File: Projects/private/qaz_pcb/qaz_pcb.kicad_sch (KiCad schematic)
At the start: 2 parts

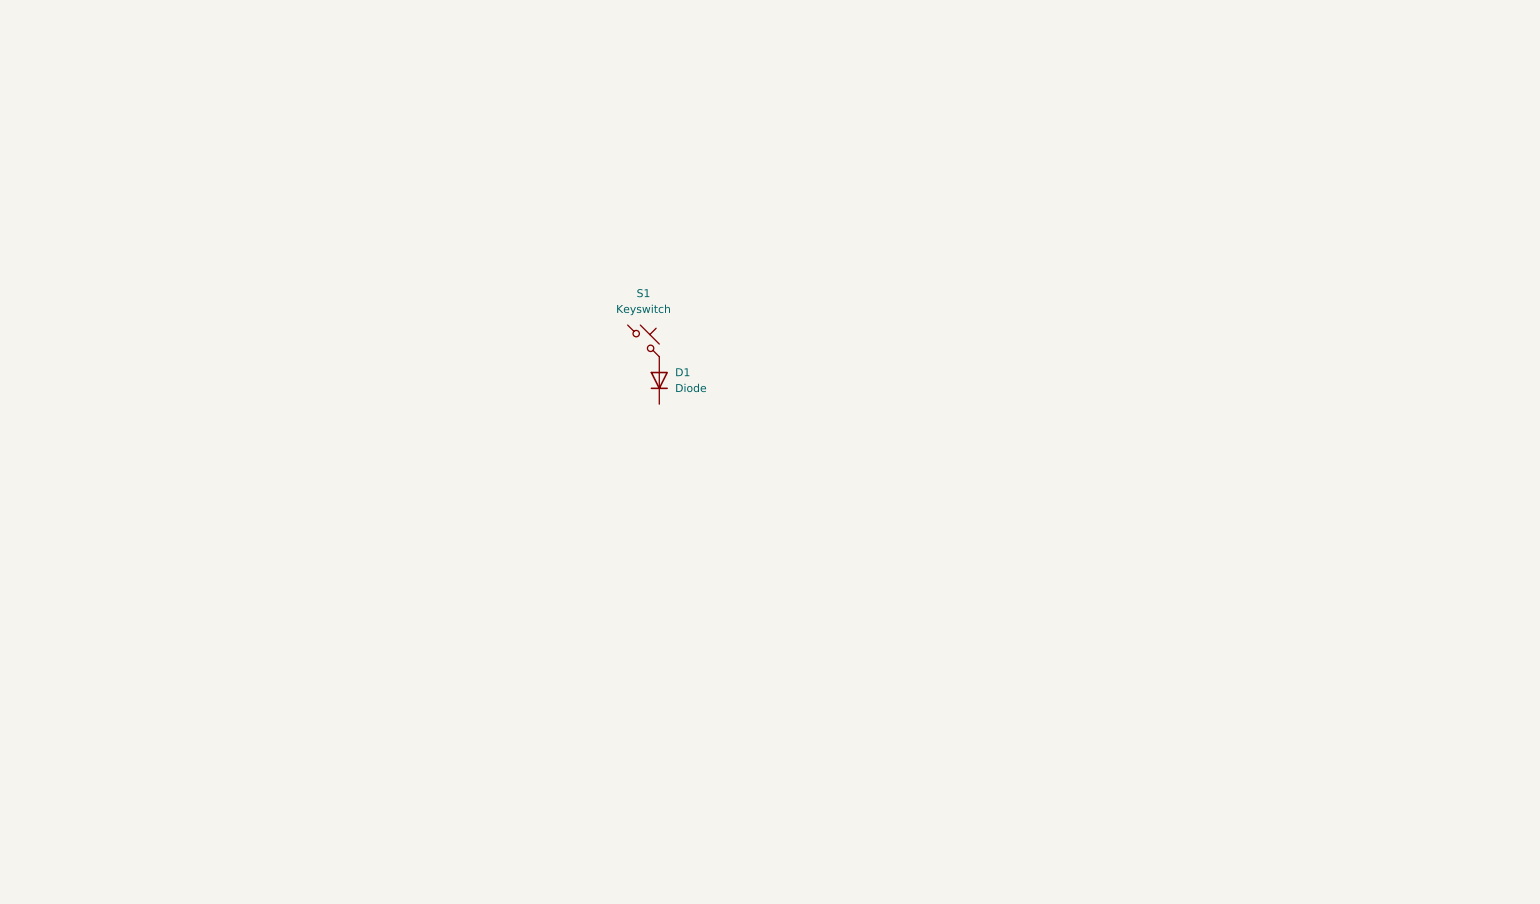
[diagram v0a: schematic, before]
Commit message: update
- aligned everything
- only connections need to be traced
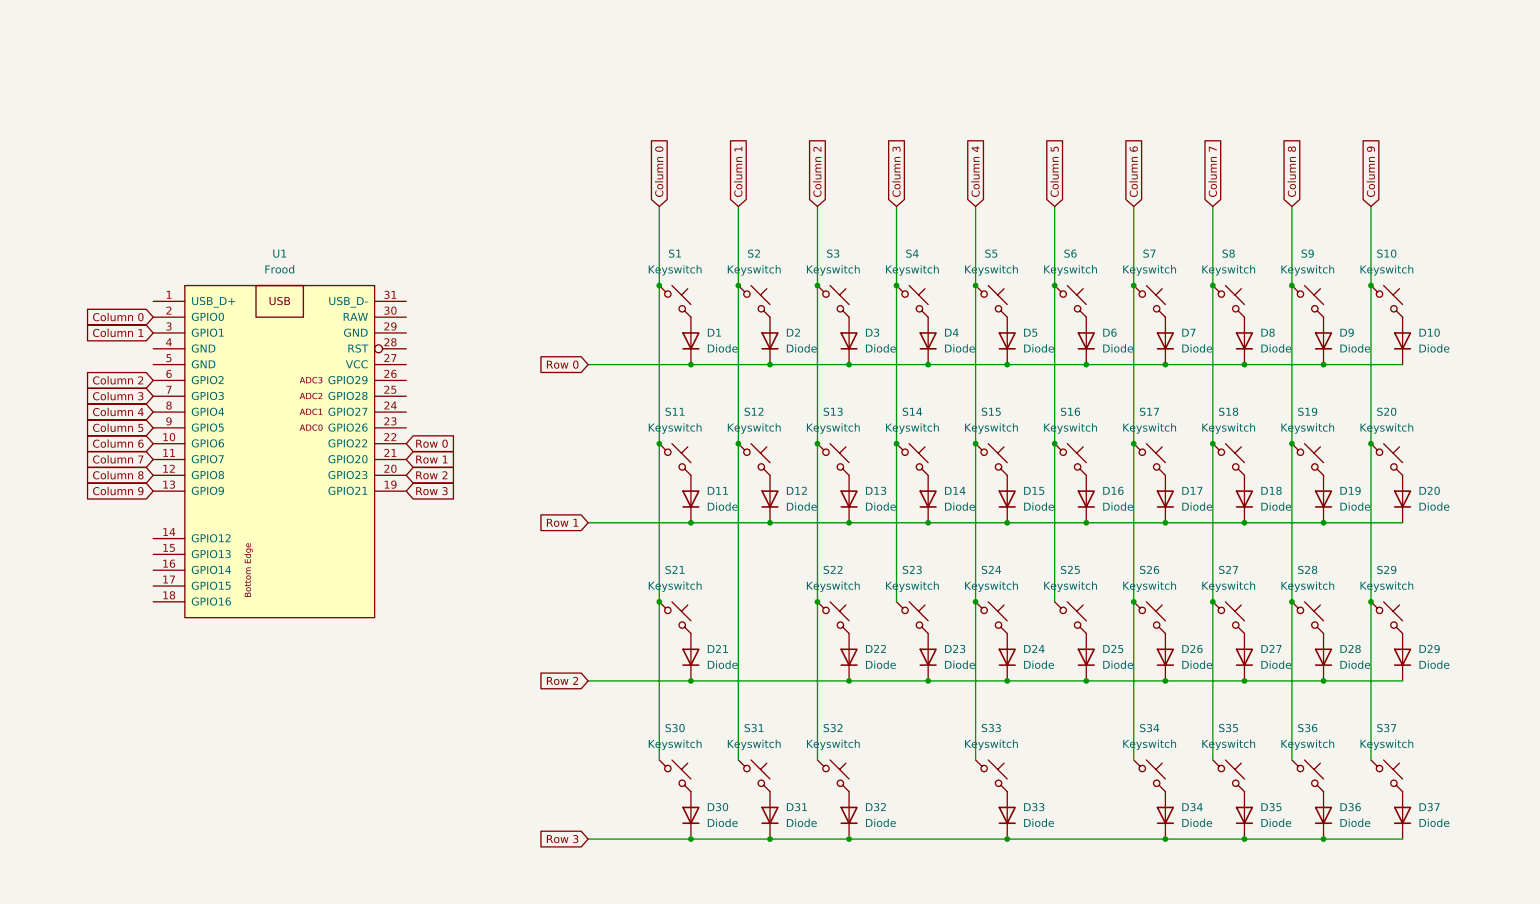
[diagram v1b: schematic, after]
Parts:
- added D10, D11, D12, D13, D14, D15, D16, D17, D18, D19, D2, D20, D21, D22, D23, D24, D25, D26, D27, D28, D29, D3, D30, D31, D32, D33, D34, D35, D36, D37, D4, D5, D6, D7, D8, D9: Diode, ScottoKeebs_Components:Diode_SOD-123, symbol Kunsteak:Placeholder_Diode
- added S10, S11: Keyswitch, ScottoKeebs_Hotswap:Hotswap_MX_1.25u, symbol Kunsteak:Placeholder_Keyswitch
- added S12, S13, S14, S15, S16, S17, S18, S19, S2, S20, S22, S23, S24, S25, S26, S27, S28, S3, S30, S31, S32, S35, S36, S37, S4, S5, S6, S7, S8, S9: Keyswitch, ScottoKeebs_Hotswap:Hotswap_MX_1.00u, symbol Kunsteak:Placeholder_Keyswitch
- added S21: Keyswitch, ScottoKeebs_Hotswap:Hotswap_MX_1.75u, symbol Kunsteak:Placeholder_Keyswitch
- added S29: Keyswitch, ScottoKeebs_Hotswap:Hotswap_MX_1.50u, symbol Kunsteak:Placeholder_Keyswitch
- added S33: Keyswitch, ScottoKeebs_Hotswap:Hotswap_MX_2.25u, symbol Kunsteak:Placeholder_Keyswitch
- added S34: Keyswitch, ScottoKeebs_Hotswap:Hotswap_MX_2.00u, symbol Kunsteak:Placeholder_Keyswitch
- added U1: Frood, footprints:Frood_PinHeader_2x13+5_P2.54mm_Labels_Top, symbol 42Keebs:Frood
- D1: footprint (none) -> ScottoKeebs_Components:Diode_SOD-123
- S1: footprint (none) -> ScottoKeebs_Hotswap:Hotswap_MX_1.00u
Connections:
- net Column 0: now reaches S1.1
- net Column 0: now also S11.1, S21.1, S30.1, U1.2 (GPIO0)
- net Row 0: now reaches D1.1 (K)
- net Row 0: now also D10.1 (K), D2.1 (K), D3.1 (K), D4.1 (K), D5.1 (K), D6.1 (K), D7.1 (K), D8.1 (K), D9.1 (K), U1.22 (GPIO22)
- new net: D15.2 (A), S15.2
- new net: D8.2 (A), S8.2
- new net: D7.2 (A), S7.2
- new net: D20.2 (A), S20.2
- new net: D35.2 (A), S35.2
- new net: D26.2 (A), S26.2
- new net: D29.2 (A), S29.2
- new net: D22.2 (A), S22.2
- new net: D34.2 (A), S34.2
- new net: D12.2 (A), S12.2
- new net: D27.2 (A), S27.2
- new net: D24.2 (A), S24.2
- new net: D32.2 (A), S32.2
- new net: D9.2 (A), S9.2
- new net: D31.2 (A), S31.2
- new net: D2.2 (A), S2.2
- new net: D5.2 (A), S5.2
- new net: D4.2 (A), S4.2
- new net: D23.2 (A), S23.2
- new net: D10.2 (A), S10.2
- new net: D37.2 (A), S37.2
- new net: D19.2 (A), S19.2
- new net: D28.2 (A), S28.2
- new net: D6.2 (A), S6.2
- new net: D17.2 (A), S17.2
- new net: D25.2 (A), S25.2
- new net: D16.2 (A), S16.2
- new net: D3.2 (A), S3.2
- new net: D36.2 (A), S36.2
- new net: D13.2 (A), S13.2
- new net: D21.2 (A), S21.2
- new net: D30.2 (A), S30.2
- new net: D18.2 (A), S18.2
- new net: D33.2 (A), S33.2
- new net: D14.2 (A), S14.2
- new net: D11.2 (A), S11.2
- new net Column 1: S12.1, S2.1, S31.1, U1.3 (GPIO1)
- new net Column 2: S13.1, S22.1, S3.1, S32.1, U1.6 (GPIO2)
- new net Column 3: S14.1, S23.1, S4.1, U1.7 (GPIO3)
- new net Column 4: S15.1, S24.1, S33.1, S5.1, U1.8 (GPIO4)
- new net Column 5: S16.1, S25.1, S6.1, U1.9 (GPIO5)
- new net Column 6: S17.1, S26.1, S34.1, S7.1, U1.10 (GPIO6)
- new net Column 7: S18.1, S27.1, S35.1, S8.1, U1.11 (GPIO7)
- new net Column 8: S19.1, S28.1, S36.1, S9.1, U1.12 (GPIO8)
- new net Column 9: S10.1, S20.1, S29.1, S37.1, U1.13 (GPIO9)
- new net Row 1: D11.1 (K), D12.1 (K), D13.1 (K), D14.1 (K), D15.1 (K), D16.1 (K), D17.1 (K), D18.1 (K), D19.1 (K), D20.1 (K), U1.21 (GPIO20)
- new net Row 2: D21.1 (K), D22.1 (K), D23.1 (K), D24.1 (K), D25.1 (K), D26.1 (K), D27.1 (K), D28.1 (K), D29.1 (K), U1.20 (GPIO23)
- new net Row 3: D30.1 (K), D31.1 (K), D32.1 (K), D33.1 (K), D34.1 (K), D35.1 (K), D36.1 (K), D37.1 (K), U1.19 (GPIO21)
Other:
- moved on the sheet: D1, S1

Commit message: update
- removed folders and files created with newer versions of KiCAD
- added frood-specific files
- made all the necessary changes in both schematics and pcb editor (footprints)
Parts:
- removed U1: Frood, footprints:Frood_PinHeader_2x13+5_P2.54mm_Labels_Top, symbol 42Keebs:Frood
- added U1: Frood, ScottoKeebs_MCU:Frood_PinHeader_2x13+5_P2.54mm_Labels_Top, symbol 42Keebs2:Frood
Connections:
- net Column 0: now also U1.2 (GPIO0)
- net Column 1: now also U1.3 (GPIO1)
- net Column 2: now also U1.6 (GPIO2)
- net Column 3: now also U1.7 (GPIO3)
- net Column 4: now also U1.8 (GPIO4)
- net Column 5: now also U1.9 (GPIO5)
- net Column 6: now also U1.10 (GPIO6)
- net Column 7: now also U1.11 (GPIO7)
- net Column 8: now also U1.12 (GPIO8)
- net Column 9: now also U1.13 (GPIO9)
- net Row 0: now also U1.22 (GPIO22)
- net Row 1: now also U1.21 (GPIO20)
- net Row 2: now also U1.20 (GPIO23)
- net Row 3: now also U1.19 (GPIO21)

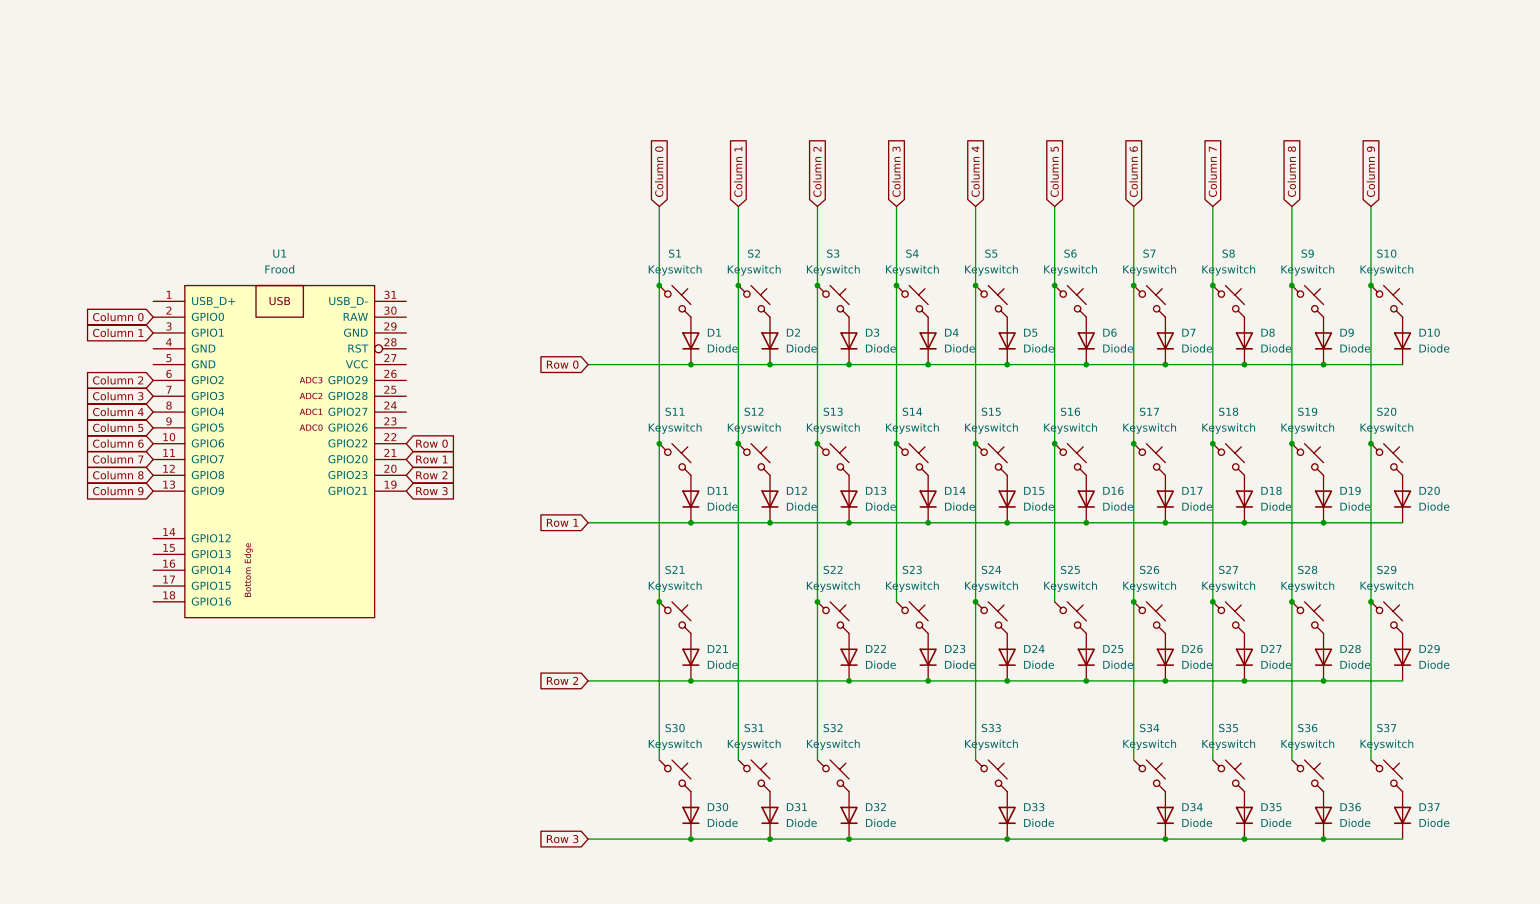
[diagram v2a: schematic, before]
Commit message: Finalised qaz pcb
- finished the traces and connections
- merged all necessary symbols, footprints, and 3d models into the ScottoKicad files and folders
- added rotary encoder for the qaz (with schematic and 3d model)
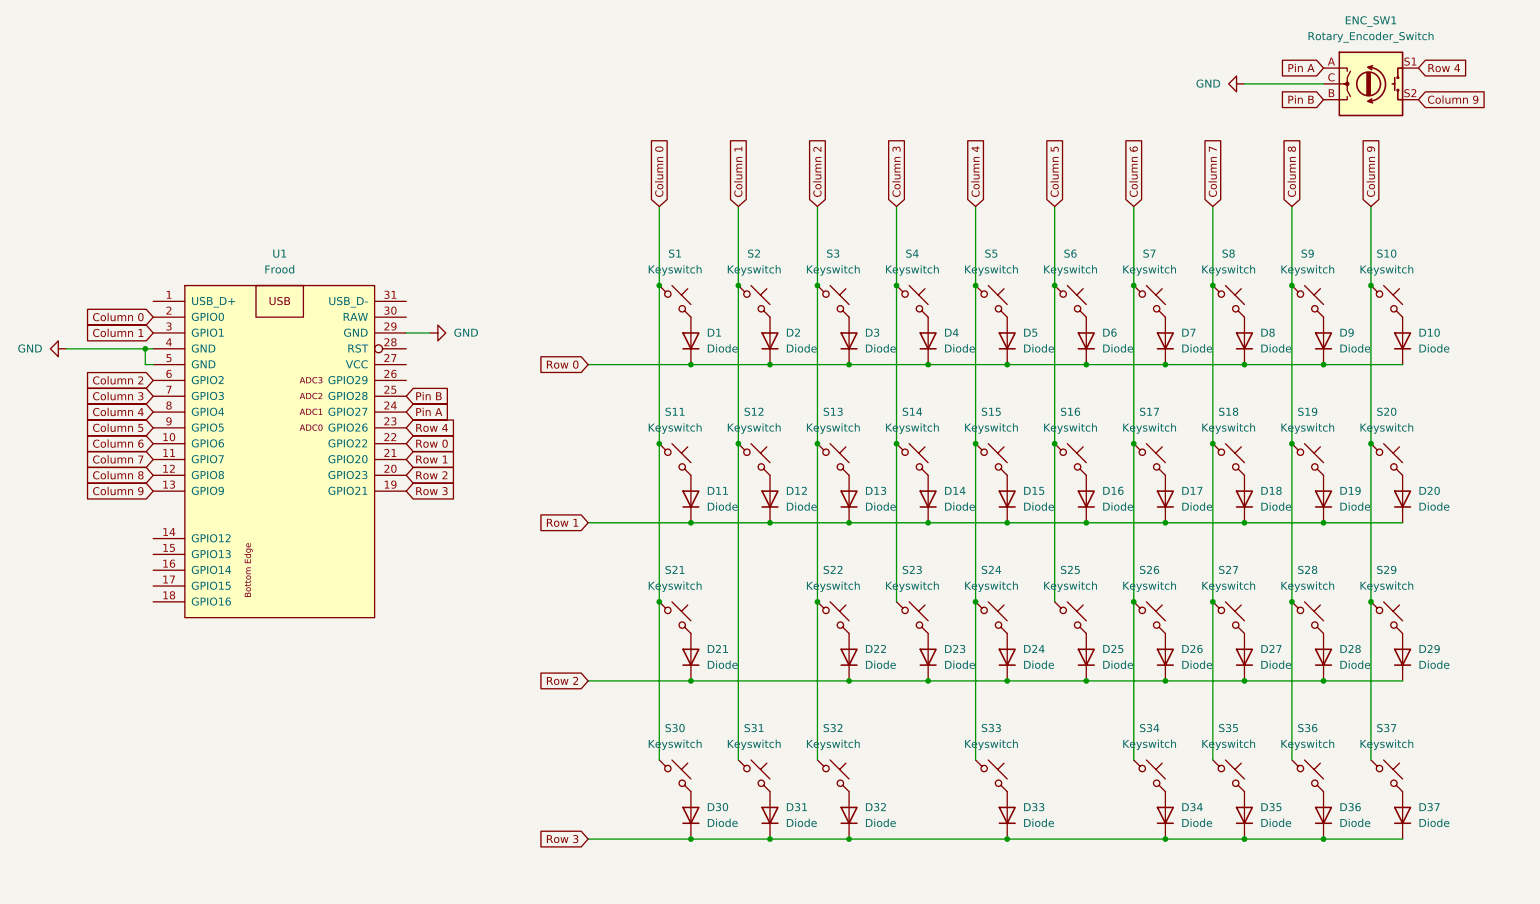
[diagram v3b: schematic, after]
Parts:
- removed U1: Frood, ScottoKeebs_MCU:Frood_PinHeader_2x13+5_P2.54mm_Labels_Top, symbol 42Keebs2:Frood
- added ENC_SW1: Rotary_Encoder_Switch, ScottoKeebs_Components:Rotary_Encoder_PEC11R-4220K-S0024, symbol ScottoKeebs:Rotary_Encoder_Switch
- added U1: Frood, ScottoKeebs_MCU:Frood_PinHeader_2x13+5_P2.54mm_Labels_Top, symbol ScottoKeebs:Frood
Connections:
- net Column 0: now also U1.2 (GPIO0)
- net Column 1: now also U1.3 (GPIO1)
- net Column 2: now also U1.6 (GPIO2)
- net Column 3: now also U1.7 (GPIO3)
- net Column 4: now also U1.8 (GPIO4)
- net Column 5: now also U1.9 (GPIO5)
- net Column 6: now also U1.10 (GPIO6)
- net Column 7: now also U1.11 (GPIO7)
- net Column 8: now also U1.12 (GPIO8)
- net Column 9: now also ENC_SW1.S2, U1.13 (GPIO9)
- net Row 0: now also U1.22 (GPIO22)
- net Row 1: now also U1.21 (GPIO20)
- net Row 2: now also U1.20 (GPIO23)
- net Row 3: now also U1.19 (GPIO21)
- new net GND: ENC_SW1.C, U1.29 (GND), U1.4 (GND), U1.5 (GND)
- new net Pin A: ENC_SW1.A, U1.24 (GPIO27)
- new net Pin B: ENC_SW1.B, U1.25 (GPIO28)
- new net Row 4: ENC_SW1.S1, U1.23 (GPIO26)

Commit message: update
- renamed everything from ScottoKeebs to Kunsteak
- only updated the footprints and symbols relevant to the qaz project (all the other ones will have to be updated once they are used)
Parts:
- D1, D10, D11, D12, D13, D14, D15, D16, D17, D18, D19, D2, D20, D21, D22, D23, D24, D25, D26, D27, D28, D29, D3, D30, D31, D32, D33, D34, D35, D36, D37, D4, D5, D6, D7, D8, D9: footprint ScottoKeebs_Components:Diode_SOD-123 -> Kunsteak_Components:Diode_SOD-123
- ENC_SW1: footprint ScottoKeebs_Components:Rotary_Encoder_PEC11R-4220K-S0024 -> Kunsteak_Components:Rotary_Encoder_PEC11R-4220K-S0024
- S1, S12, S13, S14, S15, S16, S17, S18, S19, S2, S20, S22, S23, S24, S25, S26, S27, S28, S3, S30, S31, S32, S35, S36, S37, S4, S5, S6, S7, S8, S9: footprint ScottoKeebs_Hotswap:Hotswap_MX_1.00u -> Kunsteak_Hotswap:Hotswap_MX_1.00u
- S10, S11: footprint ScottoKeebs_Hotswap:Hotswap_MX_1.25u -> Kunsteak_Hotswap:Hotswap_MX_1.25u
- S21: footprint ScottoKeebs_Hotswap:Hotswap_MX_1.75u -> Kunsteak_Hotswap:Hotswap_MX_1.75u
- S29: footprint ScottoKeebs_Hotswap:Hotswap_MX_1.50u -> Kunsteak_Hotswap:Hotswap_MX_1.00u
- S33: footprint ScottoKeebs_Hotswap:Hotswap_MX_2.25u -> Kunsteak_Hotswap:Hotswap_MX_2.25u
- S34: footprint ScottoKeebs_Hotswap:Hotswap_MX_2.00u -> Kunsteak_Hotswap:Hotswap_MX_2.00u
- U1: footprint ScottoKeebs_MCU:Frood_PinHeader_2x13+5_P2.54mm_Labels_Top -> Kunsteak_MCU:Frood_PinHeader_2x13+5_P2.54mm_Labels_Top

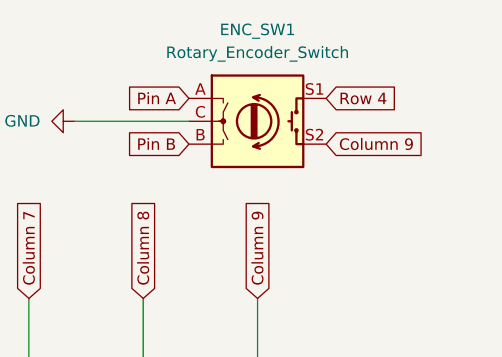
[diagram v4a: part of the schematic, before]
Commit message: update
- fixed missing diode for rotary encoder
TODO:
- add mounting holes
- create case
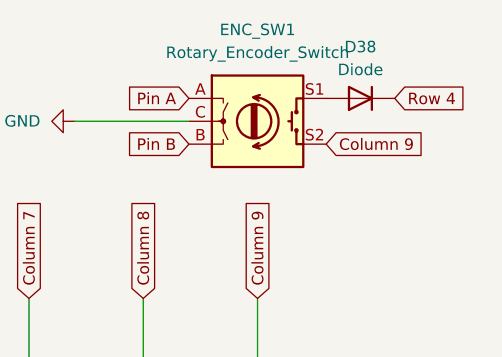
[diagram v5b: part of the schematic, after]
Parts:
- added D38: Diode, Kunsteak_Components:Diode_SOD-123, symbol Kunsteak:Placeholder_Diode
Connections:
- net Row 4: now also D38.1 (K); no longer ENC_SW1.S1
- new net: D38.2 (A), ENC_SW1.S1
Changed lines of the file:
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@@
     )
   )
-  (global_label "Row 4" (shape input) (at 256.54 28.575 0) (fields_autoplaced)
+  (global_label "Row 4" (shape input) (at 264.16 28.575 0) (fields_autoplaced)
     (effects (font (size 1.27 1.27)) (justify left))
-    (property "Intersheetrefs" "${INTERSHEET_REFS}" (at 265.4518 28.575 0)
+    (property "Intersheetrefs" "${INTERSHEET_REFS}" (at 273.0718 28.575 0)
       (effects (font (size 1.27 1.27)) (justify left) hide)
     )
@@
         )
       )
+    )
+  )
+  (symbol (lib_id "Kunsteak:Placeholder_Diode") (at 260.35 28.575 180) (unit 1)
+    (in_bom yes) (on_board yes) (dnp no) (fields_autoplaced)
+    (property "Reference" "D38" (at 260.35 22.86 0)
+      (effects (font (size 1.27 1.27)))
+    )
+    (property "Value" "Diode" (at 260.35 25.4 0)
+      (effects (font (size 1.27 1.27)))
+    )
+    (property "Footprint" "Kunsteak_Components:Diode_SOD-123" (at 260.35 28.575 0)
+      (effects (font (size 1.27 1.27)) hide)
+    )
+    (property "Datasheet" "" (at 260.35 28.575 0)
+      (effects (font (size 1.27 1.27)) hide)
+    )
+    (property "Sim.Device" "D" (at 260.35 28.575 0)
+      (effects (font (size 1.27 1.27)) hide)
+    )
+    (property "Sim.Pins" "1=K 2=A" (at 260.35 28.575 0)
+      (effects (font (size 1.27 1.27)) hide)
+    )
+    (pin "2")
+    (pin "1")
+    (instances
+      (project "qaz_pcb"
+        (path "/83dc6458-aeb5-4d2b-88e5-b34cb43c75a7"
+          (reference "D38") (unit 1)
+        )
+      )
